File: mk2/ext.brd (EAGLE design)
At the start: 11.4 x 55.9 mm, 3 parts

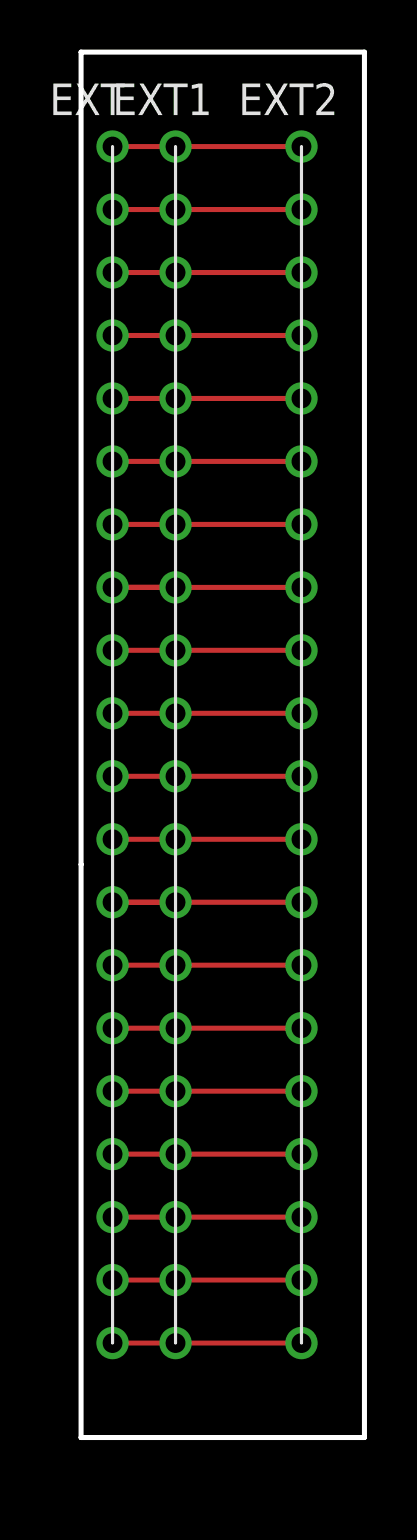
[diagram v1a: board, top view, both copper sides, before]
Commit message: [update fonts]
	- change the size and font of board texts
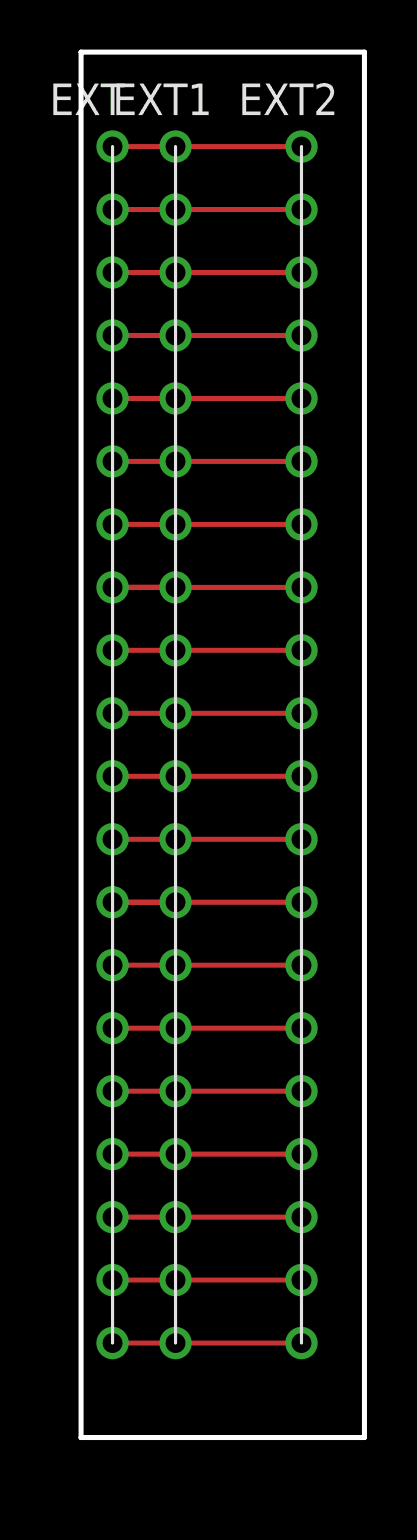
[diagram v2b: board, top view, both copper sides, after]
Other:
- outline, holes or cut-outs redrawn
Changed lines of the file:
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@@
 <layer number="21" name="tPlace" color="7" fill="1" visible="no" active="yes"/>
 <layer number="22" name="bPlace" color="7" fill="1" visible="no" active="yes"/>
-<layer number="23" name="tOrigins" color="15" fill="1" visible="yes" active="yes"/>
+<layer number="23" name="tOrigins" color="15" fill="1" visible="no" active="yes"/>
 <layer number="24" name="bOrigins" color="15" fill="1" visible="no" active="yes"/>
 <layer number="25" name="tNames" color="7" fill="1" visible="no" active="yes"/>
@@
 <plain>
 <wire x1="1.27" y1="0.762" x2="12.7" y2="0.762" width="0.2032" layer="20"/>
-<text x="7.62" y="52.578" size="0.6096" layer="48" align="center">TX0</text>
-<text x="7.62" y="50.038" size="0.6096" layer="48" align="center">RX0</text>
-<text x="7.62" y="47.498" size="0.6096" layer="48" align="center">SCL</text>
-<text x="7.62" y="44.958" size="0.6096" layer="48" align="center">SDA</text>
-<text x="7.62" y="42.418" size="0.6096" layer="48" align="center">MISO</text>
-<text x="7.62" y="39.878" size="0.6096" layer="48" align="center">MOSI</text>
-<text x="7.62" y="37.338" size="0.6096" layer="48" align="center">SCK</text>
-<text x="7.62" y="34.798" size="0.6096" layer="48" align="center">AIN0</text>
-<text x="7.62" y="32.258" size="0.6096" layer="48" align="center">GND</text>
-<text x="7.62" y="29.718" size="0.6096" layer="48" align="center">VCC</text>
-<text x="7.62" y="27.178" size="0.6096" layer="48" align="center">TX1</text>
-<text x="7.62" y="24.638" size="0.6096" layer="48" align="center">RX1</text>
-<text x="7.62" y="22.098" size="0.6096" layer="48" align="center">SCL</text>
-<text x="7.62" y="19.558" size="0.6096" layer="48" align="center">SDA</text>
-<text x="7.62" y="17.018" size="0.6096" layer="48" align="center">OC0A</text>
-<text x="7.62" y="14.478" size="0.6096" layer="48" align="center">OC0B</text>
-<text x="7.62" y="11.938" size="0.6096" layer="48" align="center">OC1A</text>
-<text x="7.62" y="9.398" size="0.6096" layer="48" align="center">OC1B</text>
-<text x="7.62" y="6.858" size="0.6096" layer="48" align="center">GND</text>
-<text x="7.62" y="4.318" size="0.6096" layer="48" align="center">VCC</text>
+<text x="7.62" y="52.832" size="0.8128" layer="48" font="fixed" align="center">TX0</text>
+<text x="7.62" y="50.292" size="0.8128" layer="48" font="fixed" align="center">RX0</text>
+<text x="7.62" y="47.752" size="0.8128" layer="48" font="fixed" align="center">SCL</text>
+<text x="7.62" y="45.212" size="0.8128" layer="48" font="fixed" align="center">SDA</text>
+<text x="7.62" y="42.672" size="0.8128" layer="48" font="fixed" align="center">MISO</text>
+<text x="7.62" y="40.132" size="0.8128" layer="48" font="fixed" align="center">MOSI</text>
+<text x="7.62" y="37.592" size="0.8128" layer="48" font="fixed" align="center">SCK</text>
+<text x="7.62" y="35.052" size="0.8128" layer="48" font="fixed" align="center">AIN0</text>
+<text x="7.62" y="32.512" size="0.8128" layer="48" font="fixed" align="center">GND</text>
+<text x="7.62" y="29.972" size="0.8128" layer="48" font="fixed" align="center">VCC</text>
+<text x="7.62" y="27.432" size="0.8128" layer="48" font="fixed" align="center">TX1</text>
+<text x="7.62" y="24.892" size="0.8128" layer="48" font="fixed" align="center">RX1</text>
+<text x="7.62" y="22.352" size="0.8128" layer="48" font="fixed" align="center">SCL</text>
+<text x="7.62" y="19.812" size="0.8128" layer="48" font="fixed" align="center">SDA</text>
+<text x="7.62" y="17.272" size="0.8128" layer="48" font="fixed" align="center">OC0A</text>
+<text x="7.62" y="14.732" size="0.8128" layer="48" font="fixed" align="center">OC0B</text>
+<text x="7.62" y="12.192" size="0.8128" layer="48" font="fixed" align="center">OC1A</text>
+<text x="7.62" y="9.652" size="0.8128" layer="48" font="fixed" align="center">OC1B</text>
+<text x="7.62" y="7.112" size="0.8128" layer="48" font="fixed" align="center">GND</text>
+<text x="7.62" y="4.572" size="0.8128" layer="48" font="fixed" align="center">VCC</text>
 <wire x1="1.27" y1="56.642" x2="12.7" y2="56.642" width="0.2032" layer="20"/>
 <wire x1="12.7" y1="56.642" x2="12.7" y2="0.762" width="0.2032" layer="20"/>
-<wire x1="1.27" y1="0.762" x2="1.27" y2="23.876" width="0.2032" layer="20"/>
-<wire x1="1.27" y1="23.876" x2="1.27" y2="56.642" width="0.2032" layer="20"/>
+<wire x1="1.27" y1="0.762" x2="1.27" y2="56.642" width="0.2032" layer="20"/>
 </plain>
 <attributes>

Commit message: [mk2 extension uart]
	- add a uart header and tx/rx config header to the mk2.1 extension
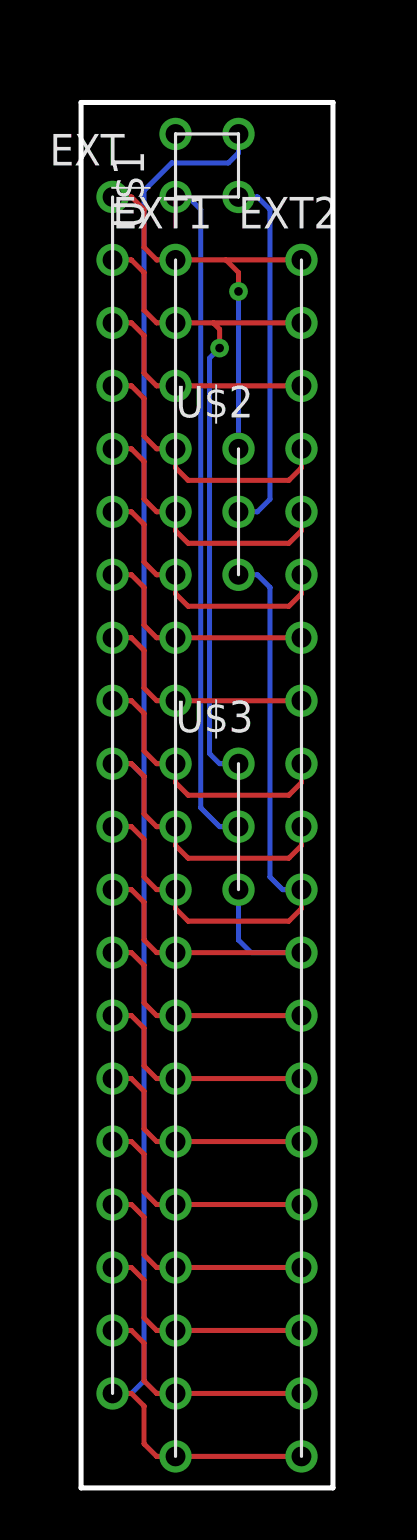
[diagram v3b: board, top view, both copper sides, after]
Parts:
- added U$1: CON_DIL_2X2, connector:CON_DIL_2X2
- added U$2, U$3: CON_DIL_3, connector:CON_DIL_3
- moved EXT1 4.57 mm to (7.62, 43.2)
- moved EXT2 4.57 mm to (12.7, 43.2)
- moved EXT 2.03 mm to (5.08, 45.7)
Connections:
- removed net EXT_GND0: EXT.P$9, EXT1.P$9, EXT2.P$9
- removed net EXT_GND1: EXT.P$19, EXT1.P$19, EXT2.P$19
- removed net EXT_VCC0: EXT.P$10, EXT1.P$10, EXT2.P$10
- removed net EXT_VCC1: EXT.P$20, EXT1.P$20, EXT2.P$20
- new net GND: EXT.P$19, EXT.P$9, EXT1.P$19, EXT1.P$9, EXT2.P$19, EXT2.P$9, U$1.P$3
- new net RX: U$1.P$1, U$3.P$2
- new net TX: U$1.P$2, U$2.P$2
- new net VCC: EXT.P$10, EXT.P$20, EXT1.P$10, EXT1.P$20, EXT2.P$10, EXT2.P$20, U$1.P$4
- net EXT_RX0: now also U$3.P$1
- net EXT_RX1: now also U$3.P$3
- net EXT_TX0: now also U$2.P$1
- net EXT_TX1: now also U$2.P$3
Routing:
- net VCC: track 0.00 -> 77.2 mm
- net RX: track 0.00 -> 27.2 mm
- net GND: track 0.00 -> 21.1 mm
- net EXT_RX0: track 7.62 -> 28.5 mm, vias 0 -> 1
- net EXT_TX1: track 7.62 -> 26.2 mm
- net TX: track 0.00 -> 14.6 mm
- net EXT_TX0: track 7.62 -> 17.4 mm, vias 0 -> 1
- net EXT_VCC1: track 7.62 -> 0.00 mm
- net EXT_VCC0: track 7.62 -> 0.00 mm
- net EXT_GND1: track 7.62 -> 0.00 mm
- net EXT_GND0: track 7.62 -> 0.00 mm
- net EXT_RX1: track 7.62 -> 14.3 mm
- net EXT_MOSI: track 7.62 -> 11.5 mm
- net EXT_MISO: track 7.62 -> 11.5 mm
- net EXT_SDA0: track 7.62 -> 11.5 mm
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- added copper zone on layer 1, net GND
- added copper zone on layer 16, net GND
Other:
- board size 11.4 x 55.9 mm -> 10.2 x 55.9 mm
- board text added: "RX"
- board text added: "TX"
- board text removed: "AIN0"
- board text removed: "MISO"
- board text removed: "MOSI"
- board text removed: "OC0A"
- board text removed: "OC0B"
- board text removed: "OC1A"
- board text removed: "OC1B"
- board text removed: "SCK"
- board text removed: "SCL"
- board text removed: "SDA"
